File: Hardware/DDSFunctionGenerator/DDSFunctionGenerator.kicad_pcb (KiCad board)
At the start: 2 copper layers, 80 x 65 mm, 155 parts, among them J1 Conn_Coaxial, J2 USB_B_Micro, J3 DG128-5.0-02P-14-00A, J4 Conn_01x02_Female, J5 Conn_Coaxial, J6 Conn_Coaxial, J7 Conn_01x04_Male, J8 Conn_01x04_Female, J9 Conn_01x04_Female, Q1 Q_NPN_BEC, Q2 Q_NPN_BEC, Q3 Q_NPN_BEC, SW1 EN11-VSB1AQ15, T1 Transformer_1P_1S, U1 TC1107-3.3VOA, U2 L7805, U3 L78L33_SO8, U4 AD9832, U5 STM32F030K6Tx, U6 FT200XD, U7 AD8325, U8 MCP3425A0T-ECH, X1 XO91, Y1 20MHz

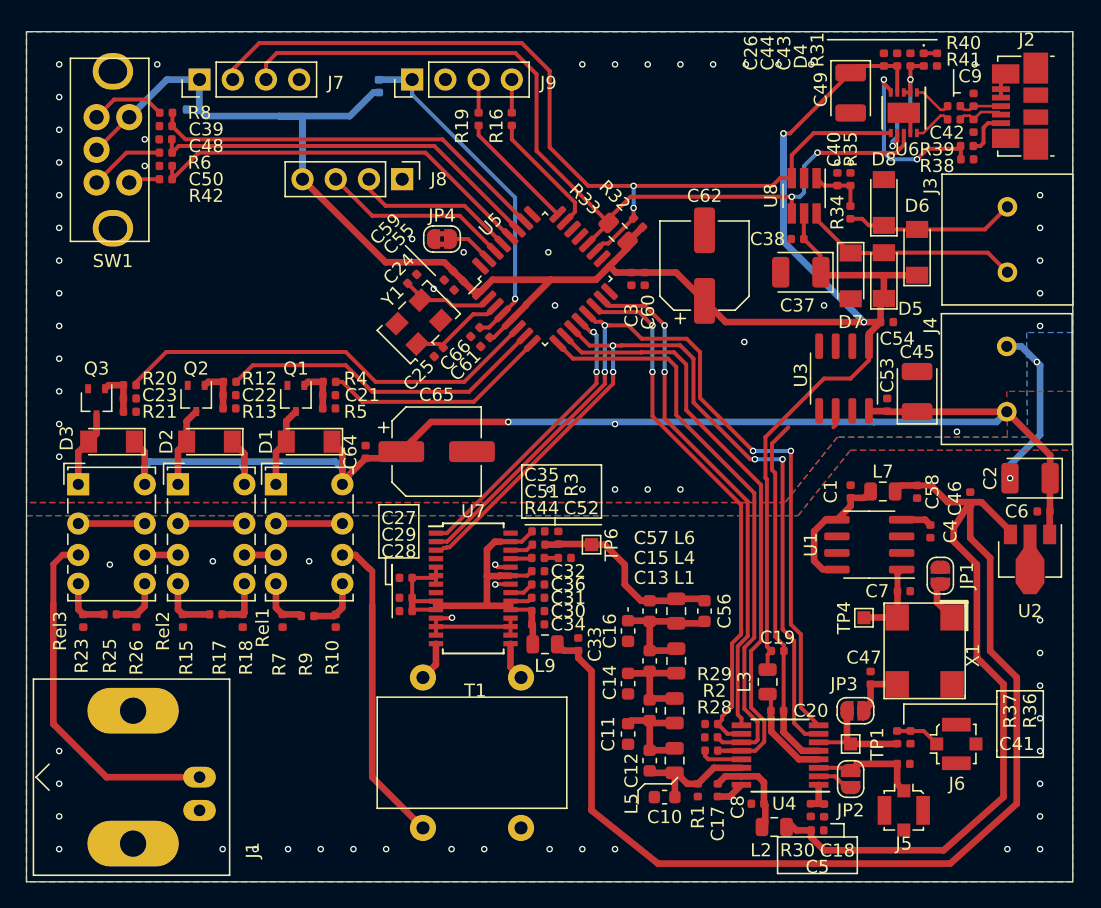
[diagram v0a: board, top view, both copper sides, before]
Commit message: Apply hardware changes after draft of mechanical overview: add mounting pad on the center of PCB, move USB closer to PCB eges, move BNC more away form PCB edge (it has a huge mounting pad for screw, it doesn't looks goood when it sticks outside from chassis). In mechanic overview, add draft ofhole for USB in chassis.
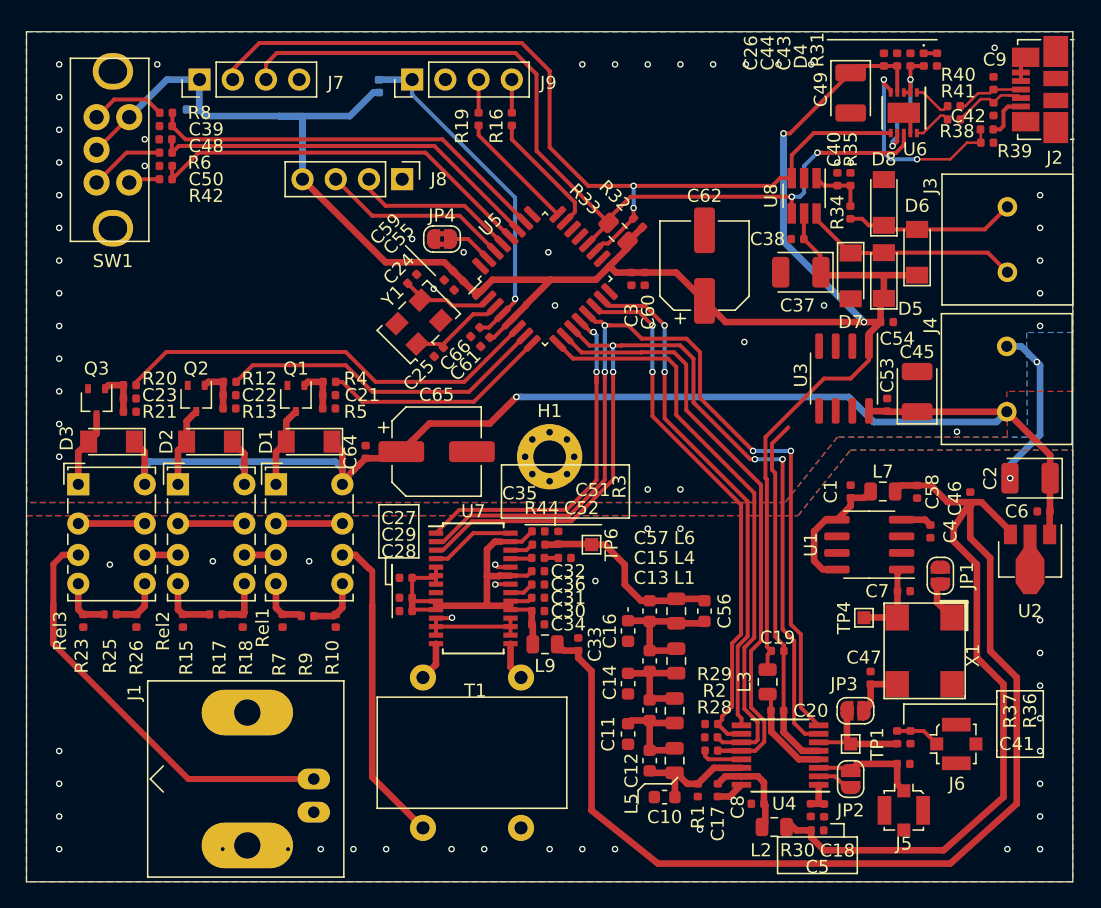
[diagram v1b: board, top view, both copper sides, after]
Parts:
- added H1: MountingHole_Pad, MountingHole:MountingHole_2.5mm_Pad_Via, F.Cu at (105.0, 102.5)
- moved J1 8.74 mm to (87.0, 127.1)
- moved C42 1.98 mm to (138.9, 75.9)
- moved C9 1.98 mm to (138.9, 73.9)
- moved J2 1.98 mm to (142.5, 74.4)
- moved R38 1.98 mm to (138.4, 77.5)
- moved R39 1.98 mm to (138.5, 78.5)
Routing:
- net Net-(J1-Pad1): track 27.3 -> 32.5 mm
- net GND: track 61.0 -> 66.2 mm, vias 77 -> 78
- net SPI1_CS_AMPLIFIER: track 22.8 -> 27.6 mm
- net SPI1_SCK: track 66.8 -> 71.1 mm
- net SPI1_MOSI: track 66.4 -> 70.6 mm
- net /ComputerInterface/D-: track 3.66 -> 6.11 mm
- net Net-(R38-Pad2): track 14.3 -> 16.3 mm
- net /ComputerInterface/D+: track 3.35 -> 5.16 mm
- net 9V: track 106.9 -> 108.4 mm, vias 2 -> 1

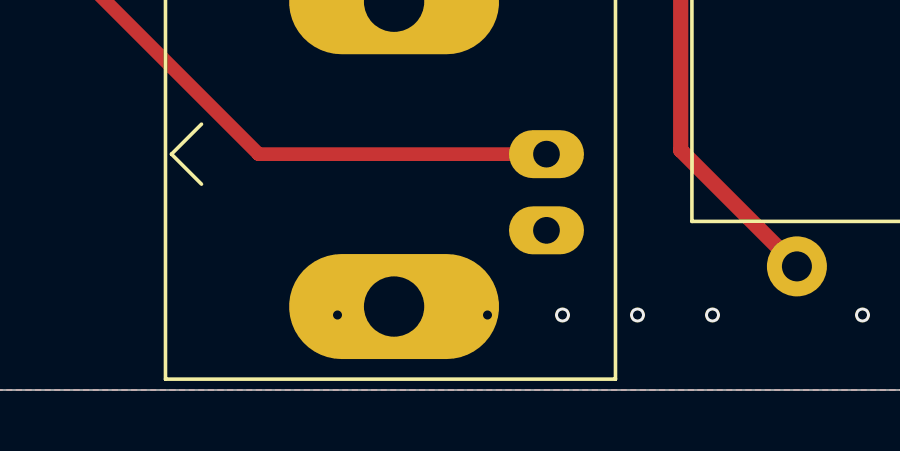
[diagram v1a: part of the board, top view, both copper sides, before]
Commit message: Remove pointless vias.
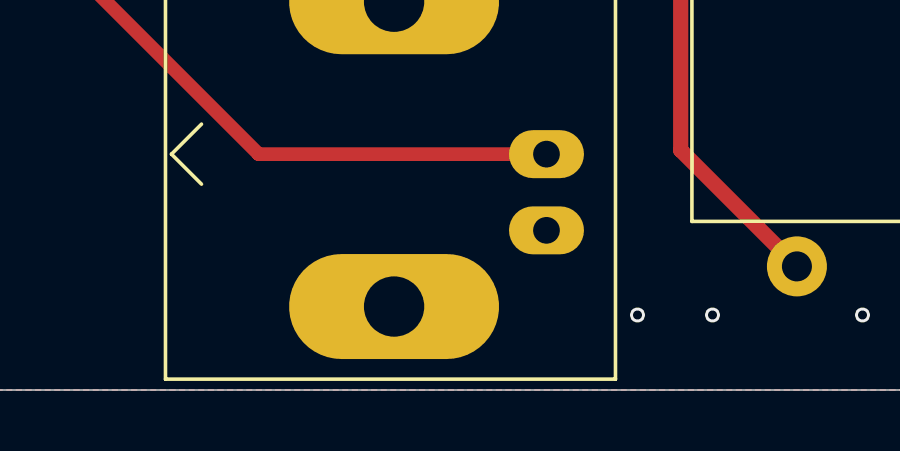
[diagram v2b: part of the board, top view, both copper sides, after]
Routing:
- net GND: vias 78 -> 74
